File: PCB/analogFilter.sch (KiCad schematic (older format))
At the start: 10 parts, among them U3 MCP6004

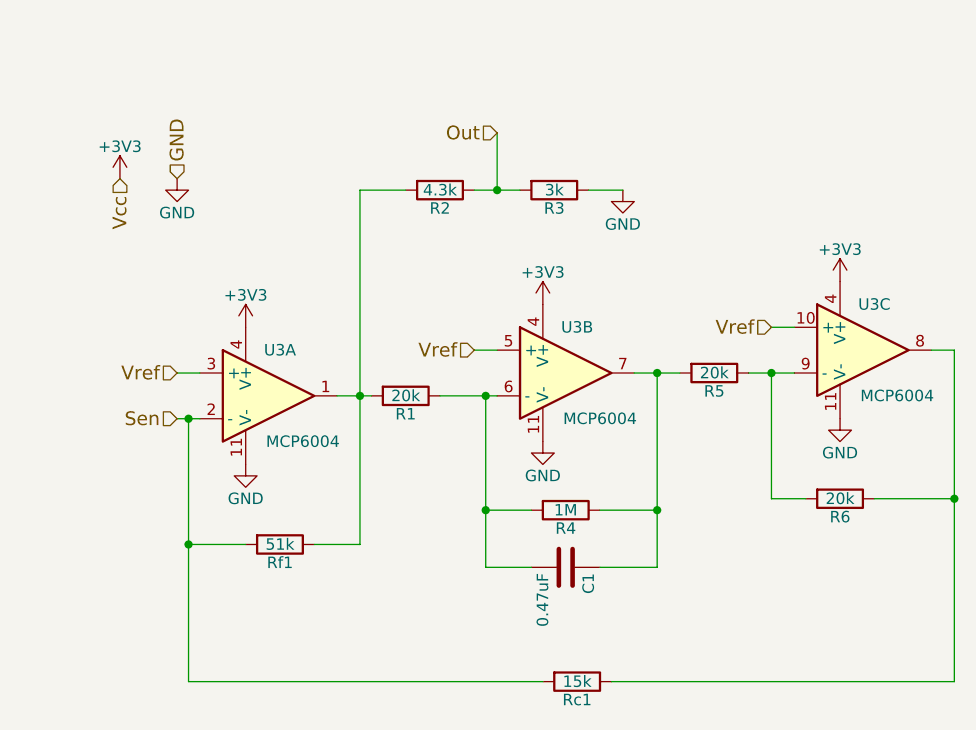
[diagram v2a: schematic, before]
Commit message: Pulled in RFM69 library, modified to support teensy
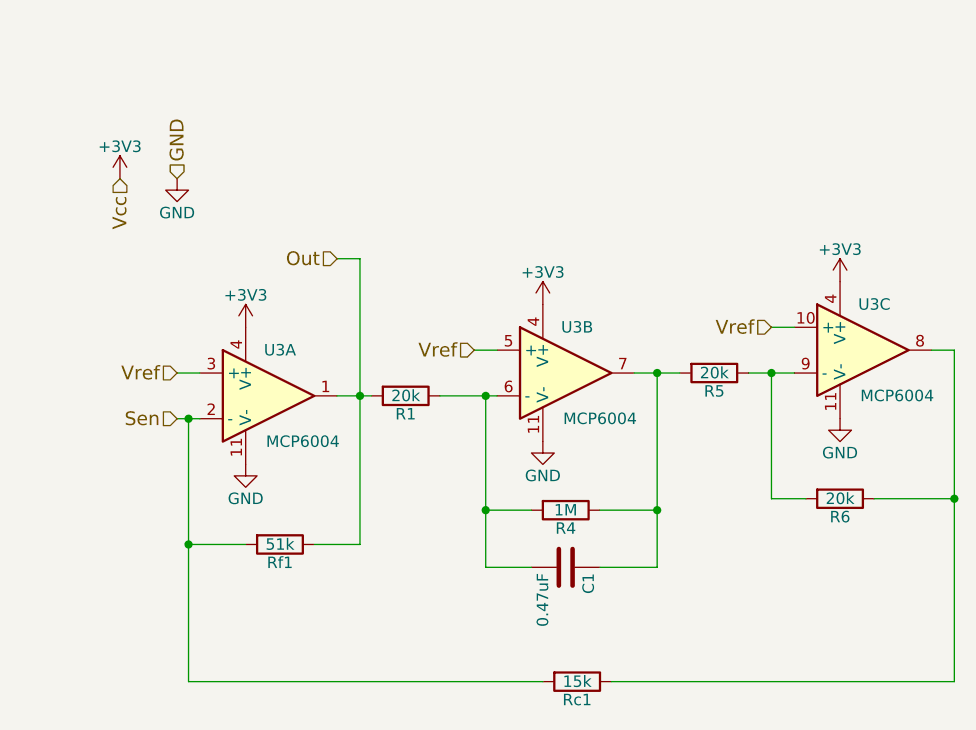
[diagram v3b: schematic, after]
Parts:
- removed R2: 4.3k, Resistors_ThroughHole:R_Axial_DIN0207_L6.3mm_D2.5mm_P7.62mm_Horizontal, symbol R
- removed R3: 3k, Resistors_ThroughHole:R_Axial_DIN0207_L6.3mm_D2.5mm_P7.62mm_Horizontal, symbol R
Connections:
- net Out: now also R1.2, Rf1.1, U3.1
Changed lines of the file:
@@
 AR Path="/5941B2B4/5941D64A" Ref="#PWR032"  Part="1"
 AR Path="/5941F948/5941D64A" Ref="#PWR041"  Part="1"
-F 0 "#PWR041" H 4000 3700 50  0001 C CNN
+F 0 "#PWR032" H 4000 3700 50  0001 C CNN
 F 1 "GND" H 4000 3800 50  0000 C CNN
 F 2 "" H 4000 3950 50  0000 C CNN
@@
 AR Path="/5941B2B4/5941D650" Ref="#PWR033"  Part="1"
 AR Path="/5941F948/5941D650" Ref="#PWR042"  Part="1"
-F 0 "#PWR042" H 5300 3600 50  0001 C CNN
+F 0 "#PWR033" H 5300 3600 50  0001 C CNN
 F 1 "GND" H 5300 3700 50  0000 C CNN
 F 2 "" H 5300 3850 50  0000 C CNN
@@
 AR Path="/5941B2B4/5941D656" Ref="#PWR034"  Part="1"
 AR Path="/5941F948/5941D656" Ref="#PWR043"  Part="1"
-F 0 "#PWR043" H 6600 3500 50  0001 C CNN
+F 0 "#PWR034" H 6600 3500 50  0001 C CNN
 F 1 "GND" H 6600 3600 50  0000 C CNN
 F 2 "" H 6600 3750 50  0000 C CNN
@@
 AR Path="/5941B2B4/5941D65C" Ref="#PWR035"  Part="1"
 AR Path="/5941F948/5941D65C" Ref="#PWR044"  Part="1"
-F 0 "#PWR044" H 4000 3200 50  0001 C CNN
+F 0 "#PWR035" H 4000 3200 50  0001 C CNN
 F 1 "+3V3" H 4000 3490 50  0000 C CNN
 F 2 "" H 4000 3350 50  0000 C CNN
@@
 AR Path="/5941B2B4/5941D662" Ref="#PWR036"  Part="1"
 AR Path="/5941F948/5941D662" Ref="#PWR045"  Part="1"
-F 0 "#PWR045" H 5300 3100 50  0001 C CNN
+F 0 "#PWR036" H 5300 3100 50  0001 C CNN
 F 1 "+3V3" H 5300 3390 50  0000 C CNN
 F 2 "" H 5300 3250 50  0000 C CNN
@@
 AR Path="/5941B2B4/5941D668" Ref="#PWR037"  Part="1"
 AR Path="/5941F948/5941D668" Ref="#PWR046"  Part="1"
-F 0 "#PWR046" H 6600 3000 50  0001 C CNN
+F 0 "#PWR037" H 6600 3000 50  0001 C CNN
 F 1 "+3V3" H 6600 3290 50  0000 C CNN
 F 2 "" H 6600 3150 50  0000 C CNN
@@
 	0    1    1    0
 $EndComp
-$Comp
-L R R2
-U 1 1 5941D6A3
-P 4850 2750
-AR Path="/5941B2B4/5941D6A3" Ref="R2"  Part="1"
-AR Path="/5941F948/5941D6A3" Ref="R8"  Part="1"
-F 0 "R2" V 4930 2750 50  0000 C CNN
-F 1 "4.3k" V 4850 2750 50  0000 C CNN
-F 2 "Resistors_ThroughHole:R_Axial_DIN0207_L6.3mm_D2.5mm_P7.62mm_Horizontal" V 4780 2750 50  0001 C CNN
-F 3 "" H 4850 2750 50  0000 C CNN
-	1    4850 2750
-	0    1    1    0
-$EndComp
-$Comp
-L R R3
-U 1 1 5941D6AA
-P 5350 2750
-AR Path="/5941B2B4/5941D6AA" Ref="R3"  Part="1"
-AR Path="/5941F948/5941D6AA" Ref="R9"  Part="1"
-F 0 "R3" V 5430 2750 50  0000 C CNN
-F 1 "3k" V 5350 2750 50  0000 C CNN
-F 2 "Resistors_ThroughHole:R_Axial_DIN0207_L6.3mm_D2.5mm_P7.62mm_Horizontal" V 5280 2750 50  0001 C CNN
-F 3 "" H 5350 2750 50  0000 C CNN
-	1    5350 2750
-	0    1    1    0
-$EndComp
-$Comp
-L GND #PWR038
-U 1 1 5941D6B1
-P 5650 2750
-AR Path="/5941B2B4/5941D6B1" Ref="#PWR038"  Part="1"
-AR Path="/5941F948/5941D6B1" Ref="#PWR047"  Part="1"
-F 0 "#PWR047" H 5650 2500 50  0001 C CNN
-F 1 "GND" H 5650 2600 50  0000 C CNN
-F 2 "" H 5650 2750 50  0000 C CNN
-F 3 "" H 5650 2750 50  0000 C CNN
-	1    5650 2750
-	1    0    0    -1
-$EndComp
 Wire Wire Line
 	3700 3550 3800 3550
@@
 Wire Wire Line
 	4500 4300 4300 4300
-Wire Wire Line
-	4500 2750 4500 4300
 Connection ~ 4500 3650
 Wire Wire Line
@@
 	3750 4900 5300 4900
 Connection ~ 3750 4300
-Wire Wire Line
-	5000 2750 5200 2750
-Wire Wire Line
-	4700 2750 4500 2750
-Wire Wire Line
-	5500 2750 5650 2750
-Wire Wire Line
-	5100 2500 5100 2750
-Connection ~ 5100 2750
 $Comp
 L +3V3 #PWR039
@@
 AR Path="/5941B2B4/5941DFE2" Ref="#PWR039"  Part="1"
 AR Path="/5941F948/5941DFE2" Ref="#PWR048"  Part="1"
-F 0 "#PWR048" H 3450 2550 50  0001 C CNN
+F 0 "#PWR039" H 3450 2550 50  0001 C CNN
 F 1 "+3V3" H 3450 2840 50  0000 C CNN
 F 2 "" H 3450 2700 50  0000 C CNN
@@
 AR Path="/5941B2B4/5941E011" Ref="#PWR040"  Part="1"
 AR Path="/5941F948/5941E011" Ref="#PWR049"  Part="1"
-F 0 "#PWR049" H 3700 2450 50  0001 C CNN
+F 0 "#PWR040" H 3700 2450 50  0001 C CNN
 F 1 "GND" H 3700 2550 50  0000 C CNN
 F 2 "" H 3700 2700 50  0000 C CNN
@@
 Text HLabel 3700 3750 0    60   Input ~ 0
 Sen
-Text HLabel 5100 2500 0    60   Input ~ 0
+Text HLabel 4400 3050 0    60   Input ~ 0
 Out
+Wire Wire Line
+	4400 3050 4500 3050
+Wire Wire Line
+	4500 3050 4500 4300
 $EndSCHEMATC

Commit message: minor pcb and BOM adjustments
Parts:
- Rc1: value 15k -> 240k
- Rf1: value 51k -> 750k
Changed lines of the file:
@@
 $EndComp
 $Comp
-L GND #PWR032
+L GND #PWR033
 U 1 1 5941D64A
 P 4000 3950
-AR Path="/5941B2B4/5941D64A" Ref="#PWR032"  Part="1"
+AR Path="/5941B2B4/5941D64A" Ref="#PWR033"  Part="1"
 AR Path="/5941F948/5941D64A" Ref="#PWR041"  Part="1"
-F 0 "#PWR032" H 4000 3700 50  0001 C CNN
+F 0 "#PWR033" H 4000 3700 50  0001 C CNN
 F 1 "GND" H 4000 3800 50  0000 C CNN
 F 2 "" H 4000 3950 50  0000 C CNN
@@
 $EndComp
 $Comp
-L GND #PWR033
+L GND #PWR034
 U 1 1 5941D650
 P 5300 3850
-AR Path="/5941B2B4/5941D650" Ref="#PWR033"  Part="1"
+AR Path="/5941B2B4/5941D650" Ref="#PWR034"  Part="1"
 AR Path="/5941F948/5941D650" Ref="#PWR042"  Part="1"
-F 0 "#PWR033" H 5300 3600 50  0001 C CNN
+F 0 "#PWR034" H 5300 3600 50  0001 C CNN
 F 1 "GND" H 5300 3700 50  0000 C CNN
 F 2 "" H 5300 3850 50  0000 C CNN
@@
 $EndComp
 $Comp
-L GND #PWR034
+L GND #PWR035
 U 1 1 5941D656
 P 6600 3750
-AR Path="/5941B2B4/5941D656" Ref="#PWR034"  Part="1"
+AR Path="/5941B2B4/5941D656" Ref="#PWR035"  Part="1"
 AR Path="/5941F948/5941D656" Ref="#PWR043"  Part="1"
-F 0 "#PWR034" H 6600 3500 50  0001 C CNN
+F 0 "#PWR035" H 6600 3500 50  0001 C CNN
 F 1 "GND" H 6600 3600 50  0000 C CNN
 F 2 "" H 6600 3750 50  0000 C CNN
@@
 $EndComp
 $Comp
-L +3V3 #PWR035
+L +3V3 #PWR036
 U 1 1 5941D65C
 P 4000 3350
-AR Path="/5941B2B4/5941D65C" Ref="#PWR035"  Part="1"
+AR Path="/5941B2B4/5941D65C" Ref="#PWR036"  Part="1"
 AR Path="/5941F948/5941D65C" Ref="#PWR044"  Part="1"
-F 0 "#PWR035" H 4000 3200 50  0001 C CNN
+F 0 "#PWR036" H 4000 3200 50  0001 C CNN
 F 1 "+3V3" H 4000 3490 50  0000 C CNN
 F 2 "" H 4000 3350 50  0000 C CNN
@@
 $EndComp
 $Comp
-L +3V3 #PWR036
+L +3V3 #PWR037
 U 1 1 5941D662
 P 5300 3250
-AR Path="/5941B2B4/5941D662" Ref="#PWR036"  Part="1"
+AR Path="/5941B2B4/5941D662" Ref="#PWR037"  Part="1"
 AR Path="/5941F948/5941D662" Ref="#PWR045"  Part="1"
-F 0 "#PWR036" H 5300 3100 50  0001 C CNN
+F 0 "#PWR037" H 5300 3100 50  0001 C CNN
 F 1 "+3V3" H 5300 3390 50  0000 C CNN
 F 2 "" H 5300 3250 50  0000 C CNN
@@
 $EndComp
 $Comp
-L +3V3 #PWR037
+L +3V3 #PWR038
 U 1 1 5941D668
 P 6600 3150
-AR Path="/5941B2B4/5941D668" Ref="#PWR037"  Part="1"
+AR Path="/5941B2B4/5941D668" Ref="#PWR038"  Part="1"
 AR Path="/5941F948/5941D668" Ref="#PWR046"  Part="1"
-F 0 "#PWR037" H 6600 3000 50  0001 C CNN
+F 0 "#PWR038" H 6600 3000 50  0001 C CNN
 F 1 "+3V3" H 6600 3290 50  0000 C CNN
 F 2 "" H 6600 3150 50  0000 C CNN
@@
 AR Path="/5941F948/5941D670" Ref="Rf2"  Part="1"
 F 0 "Rf1" V 4230 4300 50  0000 C CNN
-F 1 "51k" V 4150 4300 50  0000 C CNN
+F 1 "750k" V 4150 4300 50  0000 C CNN
 F 2 "Resistors_ThroughHole:R_Axial_DIN0207_L6.3mm_D2.5mm_P7.62mm_Horizontal" V 4080 4300 50  0001 C CNN
 F 3 "" H 4150 4300 50  0000 C CNN
@@
 AR Path="/5941F948/5941D69C" Ref="Rc2"  Part="1"
 F 0 "Rc1" V 5530 4900 50  0000 C CNN
-F 1 "15k" V 5450 4900 50  0000 C CNN
+F 1 "240k" V 5450 4900 50  0000 C CNN
 F 2 "Resistors_ThroughHole:R_Axial_DIN0207_L6.3mm_D2.5mm_P7.62mm_Horizontal" V 5380 4900 50  0001 C CNN
 F 3 "" H 5450 4900 50  0000 C CNN
@@
 P 3450 2700
 AR Path="/5941B2B4/5941DFE2" Ref="#PWR039"  Part="1"
-AR Path="/5941F948/5941DFE2" Ref="#PWR048"  Part="1"
+AR Path="/5941F948/5941DFE2" Ref="#PWR047"  Part="1"
 F 0 "#PWR039" H 3450 2550 50  0001 C CNN
 F 1 "+3V3" H 3450 2840 50  0000 C CNN
@@
 P 3700 2700
 AR Path="/5941B2B4/5941E011" Ref="#PWR040"  Part="1"
-AR Path="/5941F948/5941E011" Ref="#PWR049"  Part="1"
+AR Path="/5941F948/5941E011" Ref="#PWR048"  Part="1"
 F 0 "#PWR040" H 3700 2450 50  0001 C CNN
 F 1 "GND" H 3700 2550 50  0000 C CNN

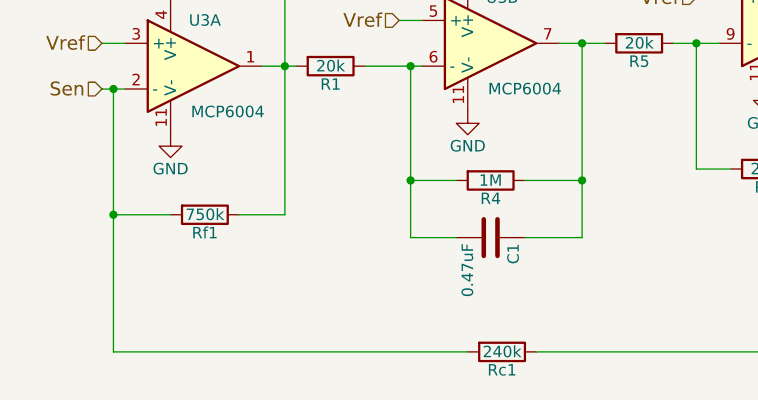
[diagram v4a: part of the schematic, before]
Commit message: Recalibrated resistor gains
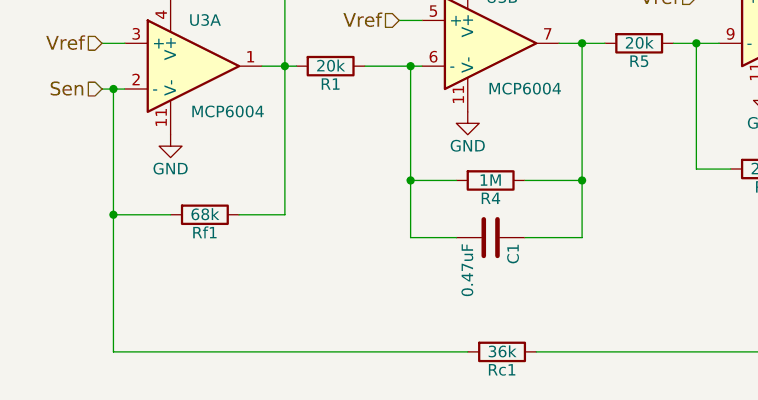
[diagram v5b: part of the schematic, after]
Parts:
- Rc1: value 240k -> 36k
- Rf1: value 750k -> 68k
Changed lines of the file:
@@
 AR Path="/5941F948/5941D670" Ref="Rf2"  Part="1"
 F 0 "Rf1" V 4230 4300 50  0000 C CNN
-F 1 "750k" V 4150 4300 50  0000 C CNN
+F 1 "68k" V 4150 4300 50  0000 C CNN
 F 2 "Resistors_ThroughHole:R_Axial_DIN0207_L6.3mm_D2.5mm_P7.62mm_Horizontal" V 4080 4300 50  0001 C CNN
 F 3 "" H 4150 4300 50  0000 C CNN
@@
 AR Path="/5941F948/5941D69C" Ref="Rc2"  Part="1"
 F 0 "Rc1" V 5530 4900 50  0000 C CNN
-F 1 "240k" V 5450 4900 50  0000 C CNN
+F 1 "36k" V 5450 4900 50  0000 C CNN
 F 2 "Resistors_ThroughHole:R_Axial_DIN0207_L6.3mm_D2.5mm_P7.62mm_Horizontal" V 5380 4900 50  0001 C CNN
 F 3 "" H 5450 4900 50  0000 C CNN

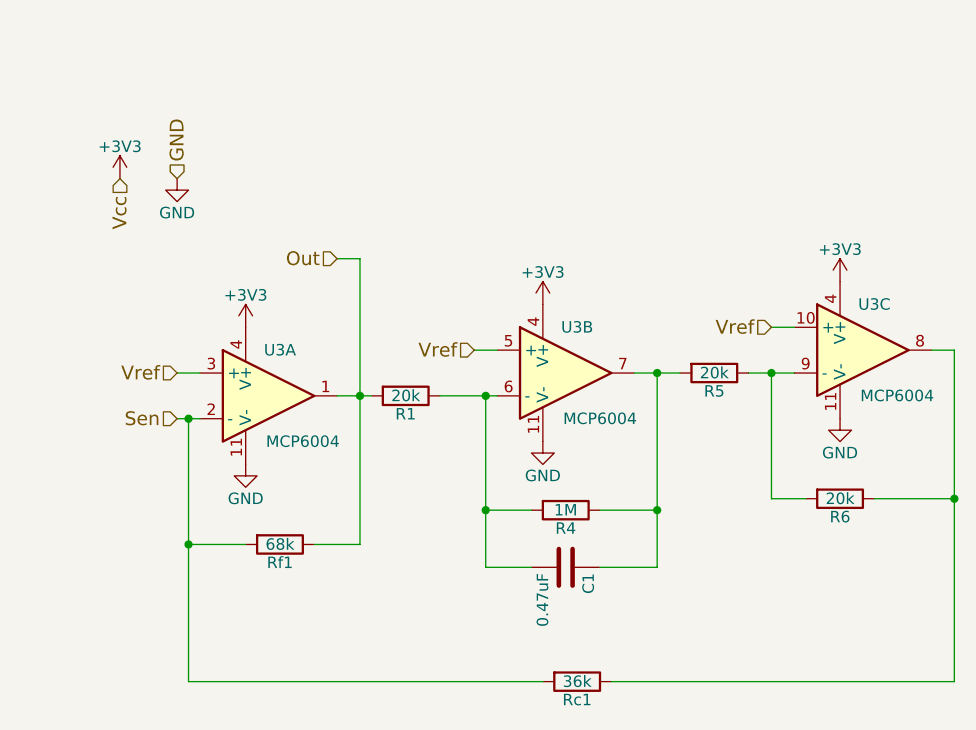
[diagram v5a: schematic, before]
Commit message: Added copper pours
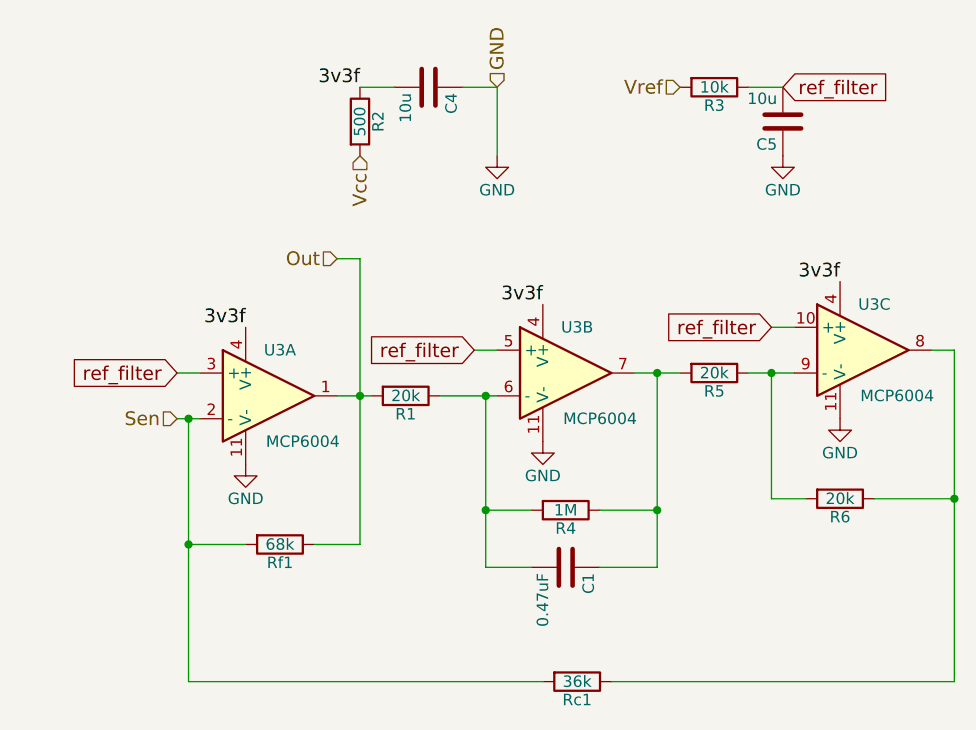
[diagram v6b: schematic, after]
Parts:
- added C4, C5: 10u, Capacitors_SMD:C_0805_HandSoldering, symbol C
- added R2: 500, Resistors_SMD:R_0603_HandSoldering, symbol R
- added R3: 10k, Resistors_SMD:R_0603_HandSoldering, symbol R
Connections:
- net GND: now also C4.1, C5.1
- net Vref: now also R3.2; no longer U3.10 (+), U3.3 (+), U3.5 (+)
- net +3V3 renamed 3v3f
- net 3v3f: now also C4.2, R2.1
- new net Vcc: R2.2
- new net ref_filter: C5.2, R3.1, U3.10 (+), U3.3 (+), U3.5 (+)
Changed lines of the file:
@@
 P 4000 3950
 AR Path="/5941B2B4/5941D64A" Ref="#PWR033"  Part="1"
-AR Path="/5941F948/5941D64A" Ref="#PWR041"  Part="1"
+AR Path="/5941F948/5941D64A" Ref="#PWR038"  Part="1"
 F 0 "#PWR033" H 4000 3700 50  0001 C CNN
 F 1 "GND" H 4000 3800 50  0000 C CNN
@@
 P 5300 3850
 AR Path="/5941B2B4/5941D650" Ref="#PWR034"  Part="1"
-AR Path="/5941F948/5941D650" Ref="#PWR042"  Part="1"
+AR Path="/5941F948/5941D650" Ref="#PWR039"  Part="1"
 F 0 "#PWR034" H 5300 3600 50  0001 C CNN
 F 1 "GND" H 5300 3700 50  0000 C CNN
@@
 P 6600 3750
 AR Path="/5941B2B4/5941D656" Ref="#PWR035"  Part="1"
-AR Path="/5941F948/5941D656" Ref="#PWR043"  Part="1"
+AR Path="/5941F948/5941D656" Ref="#PWR040"  Part="1"
 F 0 "#PWR035" H 6600 3500 50  0001 C CNN
 F 1 "GND" H 6600 3600 50  0000 C CNN
@@
 F 3 "" H 6600 3750 50  0000 C CNN
 	1    6600 3750
-	1    0    0    -1
-$EndComp
-$Comp
-L +3V3 #PWR036
-U 1 1 5941D65C
-P 4000 3350
-AR Path="/5941B2B4/5941D65C" Ref="#PWR036"  Part="1"
-AR Path="/5941F948/5941D65C" Ref="#PWR044"  Part="1"
-F 0 "#PWR036" H 4000 3200 50  0001 C CNN
-F 1 "+3V3" H 4000 3490 50  0000 C CNN
-F 2 "" H 4000 3350 50  0000 C CNN
-F 3 "" H 4000 3350 50  0000 C CNN
-	1    4000 3350
-	1    0    0    -1
-$EndComp
-$Comp
-L +3V3 #PWR037
-U 1 1 5941D662
-P 5300 3250
-AR Path="/5941B2B4/5941D662" Ref="#PWR037"  Part="1"
-AR Path="/5941F948/5941D662" Ref="#PWR045"  Part="1"
-F 0 "#PWR037" H 5300 3100 50  0001 C CNN
-F 1 "+3V3" H 5300 3390 50  0000 C CNN
-F 2 "" H 5300 3250 50  0000 C CNN
-F 3 "" H 5300 3250 50  0000 C CNN
-	1    5300 3250
-	1    0    0    -1
-$EndComp
-$Comp
-L +3V3 #PWR038
-U 1 1 5941D668
-P 6600 3150
-AR Path="/5941B2B4/5941D668" Ref="#PWR038"  Part="1"
-AR Path="/5941F948/5941D668" Ref="#PWR046"  Part="1"
-F 0 "#PWR038" H 6600 3000 50  0001 C CNN
-F 1 "+3V3" H 6600 3290 50  0000 C CNN
-F 2 "" H 6600 3150 50  0000 C CNN
-F 3 "" H 6600 3150 50  0000 C CNN
-	1    6600 3150
 	1    0    0    -1
 $EndComp
@@
 Connection ~ 3750 4300
 $Comp
-L +3V3 #PWR039
-U 1 1 5941DFE2
-P 3450 2700
-AR Path="/5941B2B4/5941DFE2" Ref="#PWR039"  Part="1"
-AR Path="/5941F948/5941DFE2" Ref="#PWR047"  Part="1"
-F 0 "#PWR039" H 3450 2550 50  0001 C CNN
-F 1 "+3V3" H 3450 2840 50  0000 C CNN
-F 2 "" H 3450 2700 50  0000 C CNN
-F 3 "" H 3450 2700 50  0000 C CNN
-	1    3450 2700
-	1    0    0    -1
-$EndComp
-$Comp
-L GND #PWR040
+L GND #PWR036
 U 1 1 5941E011
-P 3700 2700
-AR Path="/5941B2B4/5941E011" Ref="#PWR040"  Part="1"
-AR Path="/5941F948/5941E011" Ref="#PWR048"  Part="1"
-F 0 "#PWR040" H 3700 2450 50  0001 C CNN
-F 1 "GND" H 3700 2550 50  0000 C CNN
-F 2 "" H 3700 2700 50  0000 C CNN
-F 3 "" H 3700 2700 50  0000 C CNN
-	1    3700 2700
-	1    0    0    -1
-$EndComp
-Text HLabel 3450 2700 3    60   Input ~ 0
+P 5100 2600
+AR Path="/5941B2B4/5941E011" Ref="#PWR036"  Part="1"
+AR Path="/5941F948/5941E011" Ref="#PWR041"  Part="1"
+F 0 "#PWR036" H 5100 2350 50  0001 C CNN
+F 1 "GND" H 5100 2450 50  0000 C CNN
+F 2 "" H 5100 2600 50  0000 C CNN
+F 3 "" H 5100 2600 50  0000 C CNN
+	1    5100 2600
+	1    0    0    -1
+$EndComp
+Text HLabel 4500 2600 3    60   Input ~ 0
 Vcc
-Text HLabel 3700 2700 1    60   Input ~ 0
+Text HLabel 5100 2300 1    60   Input ~ 0
 GND
-Text HLabel 3700 3550 0    60   Input ~ 0
-Vref
-Text HLabel 5000 3450 0    60   Input ~ 0
-Vref
-Text HLabel 6300 3350 0    60   Input ~ 0
+Text HLabel 5900 2300 0    60   Input ~ 0
 Vref
 Text HLabel 3700 3750 0    60   Input ~ 0
@@
 Wire Wire Line
 	4500 3050 4500 4300
+$Comp
+L R R2
+U 1 1 597264A4
+P 4500 2450
+AR Path="/5941B2B4/597264A4" Ref="R2"  Part="1"
+AR Path="/5941F948/597264A4" Ref="R8"  Part="1"
+F 0 "R2" V 4580 2450 50  0000 C CNN
+F 1 "500" V 4500 2450 50  0000 C CNN
+F 2 "Resistors_SMD:R_0603_HandSoldering" V 4430 2450 50  0001 C CNN
+F 3 "" H 4500 2450 50  0000 C CNN
+	1    4500 2450
+	1    0    0    -1
+$EndComp
+$Comp
+L C C4
+U 1 1 59726523
+P 4800 2300
+AR Path="/5941B2B4/59726523" Ref="C4"  Part="1"
+AR Path="/5941F948/59726523" Ref="C6"  Part="1"
+F 0 "C4" H 4825 2400 50  0000 L CNN
+F 1 "10u" H 4825 2200 50  0000 L CNN
+F 2 "Capacitors_SMD:C_0805_HandSoldering" H 4838 2150 50  0001 C CNN
+F 3 "" H 4800 2300 50  0000 C CNN
+	1    4800 2300
+	0    1    1    0
+$EndComp
+Wire Wire Line
+	5100 2300 5100 2600
+Wire Wire Line
+	4950 2300 5100 2300
+Wire Wire Line
+	4500 2300 4650 2300
+$Comp
+L C C5
+U 1 1 5972722E
+P 6350 2450
+AR Path="/5941B2B4/5972722E" Ref="C5"  Part="1"
+AR Path="/5941F948/5972722E" Ref="C7"  Part="1"
+F 0 "C5" H 6375 2550 50  0000 L CNN
+F 1 "10u" H 6375 2350 50  0000 L CNN
+F 2 "Capacitors_SMD:C_0805_HandSoldering" H 6388 2300 50  0001 C CNN
+F 3 "" H 6350 2450 50  0000 C CNN
+	1    6350 2450
+	-1   0    0    1
+$EndComp
+Wire Wire Line
+	6200 2300 6350 2300
+$Comp
+L GND #PWR037
+U 1 1 59727314
+P 6350 2600
+AR Path="/5941B2B4/59727314" Ref="#PWR037"  Part="1"
+AR Path="/5941F948/59727314" Ref="#PWR042"  Part="1"
+F 0 "#PWR037" H 6350 2350 50  0001 C CNN
+F 1 "GND" H 6350 2450 50  0000 C CNN
+F 2 "" H 6350 2600 50  0000 C CNN
+F 3 "" H 6350 2600 50  0000 C CNN
+	1    6350 2600
+	1    0    0    -1
+$EndComp
+$Comp
+L R R3
+U 1 1 597274A4
+P 6050 2300
+AR Path="/5941B2B4/597274A4" Ref="R3"  Part="1"
+AR Path="/5941F948/597274A4" Ref="R9"  Part="1"
+F 0 "R3" V 6130 2300 50  0000 C CNN
+F 1 "10k" V 6050 2300 50  0000 C CNN
+F 2 "Resistors_SMD:R_0603_HandSoldering" V 5980 2300 50  0001 C CNN
+F 3 "" H 6050 2300 50  0000 C CNN
+	1    6050 2300
+	0    1    1    0
+$EndComp
+Text Label 4500 2300 2    60   ~ 0
+3v3f
+Text Label 4000 3350 2    60   ~ 0
+3v3f
+Text Label 5300 3250 2    60   ~ 0
+3v3f
+Text Label 6600 3150 2    60   ~ 0
+3v3f
+Text GLabel 6350 2300 2    60   Input ~ 0
+ref_filter
+Text GLabel 3700 3550 0    60   Input ~ 0
+ref_filter
+Text GLabel 5000 3450 0    60   Input ~ 0
+ref_filter
+Text GLabel 6300 3350 0    60   Input ~ 0
+ref_filter
 $EndSCHEMATC
